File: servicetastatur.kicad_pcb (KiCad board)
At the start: 2 copper layers, 113 x 60 mm, 69 parts, among them J1 Conn_01x02, J2 LCD, J3 Automat, J4 Tasten, Q1 2N3904, U1 74HC238, U17 TL7705A, U18 MC34063AP, U2 74HC00, U3 27C128, U5 74LS573, U6 74HC4094, U7 74HC4094, U8 74HC165, U9 AT24CS16-SSHM, Y1 Crystal

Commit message: stecker
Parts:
- added C22: C, Capacitor_THT:C_Axial_L3.8mm_D2.6mm_P7.50mm_Horizontal, F.Cu at (109.2, 115.2)
- J2: footprint Connector_TE-Connectivity:TE_Micro-MaTch_1-215079-6_2x08_P1.27mm_Vertical -> adp:FFC_2x08_P1mm_Vertical
- J4: footprint Connector_Molex:Molex_Nano-Fit_105313-xx06_1x06_P2.50mm_Horizontal -> adp:FFC_1x06_P2.50mm_Horizontal
- Y1: value Crystal -> 11.059
- moved R26 22.1 mm to (168.0, 140.2), turned to 90 degrees
- moved J2 21.6 mm to (111.2, 124.8)
- moved R27 20.6 mm to (163.0, 140.2), turned to 90 degrees
- moved C19 4.54 mm to (171.0, 121.0), turned to 90 degrees
- moved C12 2.69 mm to (163.5, 122.0)
- moved J1 2.51 mm to (185.5, 118.2), turned to 180 degrees
- moved R1 1.97 mm to (90.0, 129.5)
- moved R2 1.97 mm to (103.0, 129.5)
- moved C8 1.78 mm to (89.5, 76.0)
- moved R6 1.75 mm to (118.5, 130.0)
- moved U18 1.58 mm to (135.9, 130.0)
- moved R5 1.56 mm to (118.0, 123.0)
- moved D2 1.52 mm to (118.0, 126.2)
- moved C7 1.44 mm to (146.1, 122.5)
- moved Y1 1.41 mm to (96.0, 83.5)
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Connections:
- C13 pad 1: GND -> Net-(D4-K)
- C19 pad 1: unconnected-(C19-Pad1) -> Net-(C19-Pad1)
- C21 pad 1: unconnected-(C21-Pad1) -> VCC
- C5 pad 2: Net-(U9-VCC) -> VCC
- C7 pad 2: Net-(U18-Vin) -> Net-(D3-K)
- C8 pad 1: Net-(C8-Pad1) -> GND
- C9 pad 1: Net-(C8-Pad1) -> GND
- D1 pad 1: VCC -> unconnected-(D1-K-Pad1)
- D2 pad 2: GND -> unconnected-(D2-A-Pad2)
- D4 pad 1: unconnected-(D4-K-Pad1) -> Net-(D4-K)
- D4 pad 2: unconnected-(D4-A-Pad2) -> GND
- J2 pad 13: unconnected-(J2-Pin_13-Pad13) -> Net-(J2-Pin_13)
- J2 pad 15: unconnected-(J2-Pin_15-Pad15) -> VCC
- J2 pad 2: unconnected-(J2-Pin_2-Pad2) -> Net-(J2-Pin_2)
- J2 pad 5: unconnected-(J2-Pin_5-Pad5) -> D5
- J2 pad 8: unconnected-(J2-Pin_8-Pad8) -> D2
- J3 pad 1: unconnected-(J3-Pin_1-Pad1) -> GND
- J4 pad 4: unconnected-(J4-Pin_4-Pad4) -> Net-(J4-Pin_4)
- J4 pad 5: unconnected-(J4-Pin_5-Pad5) -> Net-(J4-Pin_5)
- J4 pad 6: unconnected-(J4-Pin_6-Pad6) -> Net-(J4-Pin_6)
- Q1 pad 1: unconnected-(Q1-E-Pad1) -> Net-(D2-K)
- R1 pad 1: GND -> unconnected-(R1-Pad1)
- R10 pad 1: unconnected-(R10-Pad1) -> Net-(R10-Pad1)
- R15 pad 1: unconnected-(R15-Pad1) -> Net-(D4-K)
- R15 pad 2: unconnected-(R15-Pad2) -> GND
- R17 pad 1: unconnected-(R17-Pad1) -> CLOCK
- R18 pad 1: unconnected-(R18-Pad1) -> Net-(U7-D)
- R19 pad 2: unconnected-(R19-Pad2) -> Net-(U18-DC)
- R2 pad 2: unconnected-(R2-Pad2) -> Net-(J2-Pin_2)
- R20 pad 2: Net-(R20-Pad2) -> Net-(D3-K)
- R21 pad 2: Net-(R20-Pad2) -> Net-(D3-K)
- R22 pad 1: Net-(R20-Pad2) -> Net-(D3-K)
- R22 pad 2: Net-(C12-Pad1) -> Net-(C19-Pad1)
- R23 pad 1: unconnected-(R23-Pad1) -> Net-(C12-Pad1)
- R3 pad 2: Net-(R3-Pad2) -> Net-(U18-Vfb)
- R4 pad 2: Net-(R3-Pad2) -> Net-(U18-Vfb)
- U1 pad 6: unconnected-(U1-E3-Pad6) -> Net-(U1-E3)
- U18 pad 2: GND -> unconnected-(U18-SwE-Pad2)
- U18 pad 5: unconnected-(U18-Vfb-Pad5) -> Net-(U18-Vfb)
- U18 pad 6: Net-(U18-Vin) -> Net-(D3-K)
- U18 pad 8: unconnected-(U18-DC-Pad8) -> Net-(U18-DC)
- U2 pad 1: Net-(U2-Pad1) -> Net-(R10-Pad1)
- U2 pad 12: GND -> Net-(U4-P3.3/INT1)
- U2 pad 13: Net-(U2-Pad13) -> Net-(U4-P3.3/INT1)
- U2 pad 2: Net-(U2-Pad1) -> Net-(R10-Pad1)
- U2 pad 3: Net-(U2-Pad13) -> Net-(U4-P3.3/INT1)
- U2 pad 8: unconnected-(U2-Pad8) -> Net-(U1-E3)
- U3 pad 1: unconnected-(U3-VPP-Pad1) -> A15
- U3 pad 27: unconnected-(U3-~{PGM}-Pad27) -> A14
- U3 pad 9: Net-(U3-A1) -> Net-(J2-Pin_13)
- U4 pad 15: unconnected-(U4-P3.3/INT1-Pad15) -> Net-(U4-P3.3/INT1)
- U4 pad 6: unconnected-(U4-P1.4-Pad6) -> Net-(J4-Pin_4)
- U4 pad 7: unconnected-(U4-P1.5-Pad7) -> Net-(J4-Pin_5)
- U4 pad 8: unconnected-(U4-P1.6-Pad8) -> Net-(J4-Pin_6)
- U5 pad 13: Net-(U3-A1) -> Net-(J2-Pin_13)
- U6 pad 1: unconnected-(U6-STR-Pad1) -> Net-(U6-STR)
- U6 pad 3: Net-(U6-CP) -> CLOCK
- U7 pad 1: unconnected-(U7-STR-Pad1) -> Net-(U6-STR)
- U7 pad 2: unconnected-(U7-D-Pad2) -> Net-(U7-D)
- U7 pad 3: Net-(U6-CP) -> CLOCK
- U8 pad 2: unconnected-(U8-CP-Pad2) -> CLOCK
- U9 pad 1: unconnected-(U9-NC-Pad1) -> GND
- U9 pad 2: unconnected-(U9-NC-Pad2) -> GND
- U9 pad 3: unconnected-(U9-NC-Pad3) -> GND
- U9 pad 8: Net-(U9-VCC) -> VCC
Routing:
- net GND: track 134.8 -> 520.2 mm, vias 2 -> 7
- net VCC: track 102.6 -> 299.1 mm, vias 0 -> 2
- net Net-(R10-Pad1): track 0.00 -> 110.7 mm, vias 0 -> 2
- net D5: track 42.8 -> 120.3 mm, vias 2 -> 4
- net CLOCK: track 0.00 -> 69.5 mm, vias 0 -> 2
- net Net-(D3-K): track 9.69 -> 73.0 mm
- net Net-(U1-E3): track 0.00 -> 56.6 mm, vias 0 -> 2
- net (no net): track 52.4 -> 0.00 mm, vias 2 -> 0
- net Net-(U4-P3.3/INT1): track 0.00 -> 50.2 mm, vias 0 -> 1
- net RESET: track 0.00 -> 46.5 mm
- net D4: track 45.5 -> 90.0 mm
- net D6: track 52.3 -> 96.7 mm
- net D0: track 86.5 -> 125.8 mm
- net Net-(J2-Pin_2): track 0.00 -> 38.4 mm, vias 0 -> 1
- net Net-(J4-Pin_2): track 0.00 -> 36.8 mm
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- removed copper zone on B.Cu, net GND
- removed copper zone on B.Cu, net VCC
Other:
- board size 113 x 60 mm -> 113.2 x 58 mm

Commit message: spekulation
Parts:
- moved R11 0.66 mm to (167.2, 84.0)
- moved R7 0.66 mm to (167.2, 86.5)
- moved R8 0.66 mm to (167.2, 89.0)
- moved R9 0.66 mm to (167.2, 91.8)
- moved C12 0.46 mm to (164.0, 122.0)
- moved R23 0.41 mm to (156.8, 118.0)
- moved U18 0.37 mm to (136.2, 130.0)
- moved R12 0.35 mm to (148.8, 75.8)
- moved R24 0.35 mm to (92.8, 101.2)
- moved R25 0.35 mm to (77.8, 101.2)
- moved U17 0.35 mm to (156.2, 83.2)
- moved R13 0.34 mm to (138.5, 78.0)
- moved U4 0.33 mm to (116.2, 87.2)
- moved U9 0.28 mm to (125.2, 83.2)
- moved D4 0.27 mm to (171.2, 94.5)
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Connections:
- C11 pad 2: Net-(C11-Pad2) -> RESET
- D1 pad 1: unconnected-(D1-K-Pad1) -> VCC
- R12 pad 2: Net-(C11-Pad2) -> RESET
- R13 pad 1: Net-(C11-Pad2) -> RESET
- U1 pad 1: unconnected-(U1-A0-Pad1) -> Net-(U1-A0)
- U1 pad 2: unconnected-(U1-A1-Pad2) -> Net-(U1-A1)
- U1 pad 3: unconnected-(U1-A2-Pad3) -> Net-(U1-A2)
- U3 pad 4: Net-(U3-A6) -> Net-(U1-A2)
- U3 pad 5: Net-(U3-A5) -> Net-(U1-A1)
- U3 pad 6: Net-(U3-A4) -> Net-(U1-A0)
- U5 pad 16: Net-(U3-A4) -> Net-(U1-A0)
- U5 pad 17: Net-(U3-A5) -> Net-(U1-A1)
- U5 pad 18: Net-(U3-A6) -> Net-(U1-A2)
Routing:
- net Net-(U1-A1): track 0.00 -> 44.3 mm
- net Net-(U1-A2): track 0.00 -> 35.0 mm, vias 0 -> 1
- net Net-(U3-A5): track 32.6 -> 0.00 mm
- net Net-(U1-A0): track 0.00 -> 26.0 mm
- net A15: track 28.0 -> 48.3 mm
- net unconnected-(R1-Pad1): track 0.00 -> 19.3 mm
- net A14: track 54.4 -> 69.9 mm
- net Net-(U3-A6): track 12.1 -> 0.00 mm
- net Net-(U3-A4): track 12.1 -> 0.00 mm
- net unconnected-(J2-Pin_11-Pad11): track 19.0 -> 29.2 mm
- net unconnected-(U1-A2-Pad3): track 8.21 -> 0.00 mm, vias 1 -> 0
- net SDA: track 30.9 -> 26.5 mm
- net Net-(C12-Pad1): track 24.5 -> 28.0 mm
- net GND: track 520.2 -> 521.8 mm
- net Net-(J3-Pin_5): track 27.5 -> 28.5 mm
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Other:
- board size 113.2 x 58 mm -> 113.9 x 58 mm

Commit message: layout
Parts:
- added R28: R, Resistor_THT:R_Axial_DIN0207_L6.3mm_D2.5mm_P10.16mm_Horizontal, F.Cu at (132.7, 87.6)
- added R29: R, Resistor_THT:R_Axial_DIN0207_L6.3mm_D2.5mm_P10.16mm_Horizontal, F.Cu at (130.2, 87.6)
- added R30: R, Resistor_THT:R_Axial_DIN0207_L6.3mm_D2.5mm_P10.16mm_Horizontal, F.Cu at (127.5, 87.6)
- C1: footprint Capacitor_THT:CP_Radial_D5.0mm_P2.00mm -> Capacitor_THT:CP_Radial_D5.0mm_P2.50mm
- C3: renamed from C13; value C -> 68pF
- D1: footprint Diode_THT:D_DO-15_P15.24mm_Horizontal -> adp:D_DO-15_P15mm_Horizontal
- Q1: footprint Package_TO_SOT_THT:TO-92 -> adp:TO-92
- R15: renamed from R3; value 110 Ω ±1% -> 1 kΩ ±1%
- R26, R27: value 100 kΩ ±5% -> R
- R6: value R -> 220 Ω ±5%
- U4: value ~ -> 80C31
- U9: value AT24CS16-SSHM -> 24CS16
- moved Y1 49.5 mm to (70.5, 41.0)
- moved C21 49.5 mm to (100.3, 45.4)
- moved C1 49.5 mm to (91.6, 62.9)
- moved C10 49.5 mm to (141.6, 36.0)
- moved C11 49.5 mm to (127.1, 35.8)
- moved C12 49.5 mm to (138.6, 79.5)
- moved C13 49.5 mm to (96.6, 62.0)
- moved C14 49.5 mm to (135.1, 51.0)
- moved C15 49.5 mm to (119.6, 62.0)
- moved C16 49.5 mm to (119.6, 73.0)
- moved C17 49.5 mm to (96.6, 73.0)
- moved C18 49.5 mm to (83.1, 57.5)
- moved C19 49.5 mm to (145.6, 78.5)
- moved C2 49.5 mm to (91.4, 69.5)
- moved C20 49.5 mm to (138.1, 46.0)
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- renumbered C3 to C13, R15 to R3
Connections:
- net Net-(J2-Pin_13) renamed A1
- net Net-(U1-A0) renamed A4
- net Net-(U1-A1) renamed A5
- net Net-(U1-A2) renamed A6
- net Net-(U3-A2) renamed A2
- net Net-(U3-A3) renamed A3
- net Net-(U3-A7) renamed A7
- C10 pad 2: unconnected-(C10-Pad2) -> Net-(U17-CT)
- C3 pad 2: unconnected-(C13-Pad2) -> Net-(J3-Pin_3)
- C7 pad 2: Net-(D3-K) -> Net-(U18-TC)
- D2 pad 2: unconnected-(D2-A-Pad2) -> GND
- D3 pad 1: Net-(D3-K) -> +VDC
- J2 pad 10: unconnected-(J2-Pin_10-Pad10) -> D0
- J2 pad 11: unconnected-(J2-Pin_11-Pad11) -> Net-(J2-Pin_11)
- J2 pad 12: unconnected-(J2-Pin_12-Pad12) -> A0
- J2 pad 16: unconnected-(J2-Pin_16-Pad16) -> GND
- J2 pad 2: Net-(J2-Pin_2) -> GND
- J2 pad 3: unconnected-(J2-Pin_3-Pad3) -> D7
- J2 pad 4: unconnected-(J2-Pin_4-Pad4) -> D6
- J2 pad 6: unconnected-(J2-Pin_6-Pad6) -> D4
- R1 pad 1: unconnected-(R1-Pad1) -> GND
- R2 pad 2: Net-(J2-Pin_2) -> GND
- R20 pad 2: Net-(D3-K) -> +VDC
- R21 pad 2: Net-(D3-K) -> +VDC
- R22 pad 1: Net-(D3-K) -> +VDC
- R23 pad 2: Net-(D3-K) -> +VDC
- R5 pad 1: unconnected-(R5-Pad1) -> Net-(Q1-C)
- U1 pad 7: unconnected-(U1-Y7-Pad7) -> Net-(J2-Pin_11)
- U17 pad 3: unconnected-(U17-CT-Pad3) -> Net-(U17-CT)
- U18 pad 2: unconnected-(U18-SwE-Pad2) -> GND
- U18 pad 3: unconnected-(U18-TC-Pad3) -> Net-(U18-TC)
- U18 pad 6: Net-(D3-K) -> +VDC
- U3 pad 10: Net-(U3-A0) -> A0
- U5 pad 12: Net-(U3-A0) -> A0
- U6 pad 1: Net-(U6-STR) -> Net-(D4-K)
- U7 pad 1: Net-(U6-STR) -> Net-(D4-K)
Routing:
- net GND: track 521.8 -> 698.4 mm, vias 7 -> 8
- net Net-(D3-K): track 73.3 -> 0.00 mm, vias 1 -> 0
- net +VDC: track 0.00 -> 72.9 mm, vias 0 -> 1
- net D7: track 92.8 -> 159.8 mm, vias 3 -> 4
- net D6: track 97.1 -> 159.6 mm, vias 3 -> 4
- net D4: track 90.0 -> 146.1 mm, vias 2 -> 3
- net A15: track 48.3 -> 98.3 mm
- net Net-(J2-Pin_11): track 0.00 -> 42.9 mm
- net Net-(J2-Pin_2): track 38.3 -> 0.00 mm, vias 1 -> 0
- net A0: track 0.00 -> 34.6 mm
- net Net-(D4-K): track 22.5 -> 56.4 mm, vias 0 -> 1
- net unconnected-(J2-Pin_11-Pad11): track 29.2 -> 0.00 mm
- net A14: track 69.9 -> 97.7 mm
- net A6: track 35.0 -> 62.1 mm
- net unconnected-(J2-Pin_6-Pad6): track 25.5 -> 0.00 mm, vias 1 -> 0
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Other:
- outline, holes or cut-outs redrawn
- board text added: "https://github.com/stonedDiscord/"
- board text added: "servicetastatur"
- board text removed: "8320/00020f/DN"
- board text removed: "stwirtxt"

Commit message: so hab bestellt
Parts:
- removed R26, R27, R28, R29, R30: R, Resistor_THT:R_Axial_DIN0207_L6.3mm_D2.5mm_P10.16mm_Horizontal
- added J5: Conn_01x03_Pin, Connector_PinSocket_2.54mm:PinSocket_1x03_P2.54mm_Vertical, F.Cu at (127.5, 87.6)
- added J6: Conn_01x03_Pin, Connector_PinSocket_2.54mm:PinSocket_1x03_P2.54mm_Vertical, F.Cu at (137.6, 87.6)
- R20, R21, R22: value 100 kΩ ±5% -> 1 Ω ±5%
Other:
- board text added: "JLCJLCJLCJLC"

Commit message: deko
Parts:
- D1, D3: value D -> 1N5819
- R1, R4: value 3.3 kΩ ±5% -> 3.3 kΩ
- R10, R14, R15, R7, R8, R9: value 1 kΩ ±1% -> 1 kΩ
- R11: value 10 kΩ ±5% -> 10 kΩ
- R12, R2: value 22 Ω ±5% -> 22 Ω
- R13: value 47 kΩ ±5% -> 47 kΩ
- R16: value 47 Ω ±1% -> 47 Ω
- R17, R18, R19, R5: value 270 Ω ±5% -> 270 Ω
- R20, R21, R22: value 1 Ω ±5% -> 1 Ω
- R23: value 100 Ω ±1% -> 100 Ω
- R24: value 100 kΩ ±5% -> 100 kΩ
- R25, R3: value 4.7 kΩ ±1% -> 4.7 kΩ
- R6: value 220 Ω ±5% -> 220 Ω
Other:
- outline, holes or cut-outs redrawn

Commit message: lcd gefixt
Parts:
- moved J2 15.1 mm to (71.1, 84.2), turned to 90 degrees
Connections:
- J2 pad 10: D0 -> D3
- J2 pad 11: Net-(J2-Pin_11) -> D4
- J2 pad 12: A0 -> D5
- J2 pad 13: A1 -> D6
- J2 pad 14: Net-(J2-Pin_14) -> D7
- J2 pad 2: GND -> VCC
- J2 pad 3: D7 -> Net-(J2-Pin_3)
- J2 pad 4: D6 -> A1
- J2 pad 5: D5 -> A0
- J2 pad 6: D4 -> Net-(J2-Pin_6)
- J2 pad 7: D3 -> D0
- J2 pad 8: D2 -> D1
- J2 pad 9: D1 -> D2
- R1 pad 1: GND -> VCC
- R1 pad 2: Net-(J2-Pin_14) -> Net-(J2-Pin_3)
- R2 pad 2: GND -> VCC
- U1 pad 7: Net-(J2-Pin_11) -> Net-(J2-Pin_6)
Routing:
- net GND: track 698.2 -> 617.7 mm, vias 8 -> 7
- net VCC: track 317.5 -> 377.2 mm, vias 2 -> 3
- net Net-(J2-Pin_6): track 0.00 -> 42.9 mm
- net Net-(J2-Pin_11): track 42.9 -> 0.00 mm
- net Net-(J2-Pin_3): track 0.00 -> 3.54 mm
- net Net-(J2-Pin_14): track 3.54 -> 0.00 mm

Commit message: kompakt
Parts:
- removed C12: C_Polarized, Capacitor_THT:CP_Radial_D5.0mm_P2.00mm
- removed C19: C, Capacitor_THT:CP_Radial_Tantal_D4.5mm_P2.50mm
- removed C7: C, Capacitor_THT:C_Axial_L3.8mm_D2.6mm_P7.50mm_Horizontal
- removed D2: D, Diode_THT:D_DO-15_P15.24mm_Horizontal
- removed J1: Conn_01x02, Connector_Wire:SolderWire-0.5sqmm_1x02_P4.8mm_D0.9mm_OD2.3mm
- removed J4: Tasten, adp:FFC_1x06_P2.50mm_Horizontal
- removed J5, J6: Conn_01x03_Pin, Connector_PinSocket_2.54mm:PinSocket_1x03_P2.54mm_Vertical
- removed Q1: 2N3904, adp:TO-92
- removed R12, R2: 22 Ω, Resistor_THT:R_Axial_DIN0207_L6.3mm_D2.5mm_P10.16mm_Horizontal
- removed R15: 1 kΩ, Resistor_THT:R_Axial_DIN0207_L6.3mm_D2.5mm_P10.16mm_Horizontal
- removed R19, R5: 270 Ω, Resistor_THT:R_Axial_DIN0207_L6.3mm_D2.5mm_P10.16mm_Horizontal
- removed R20, R21, R22: 1 Ω, Resistor_THT:R_Axial_DIN0207_L6.3mm_D2.5mm_P10.16mm_Horizontal
- removed R23: 100 Ω, Resistor_THT:R_Axial_DIN0207_L6.3mm_D2.5mm_P10.16mm_Horizontal
- removed R24: 100 kΩ, Resistor_THT:R_Axial_DIN0207_L6.3mm_D2.5mm_P10.16mm_Horizontal
- removed R4: 3.3 kΩ, Resistor_THT:R_Axial_DIN0207_L6.3mm_D2.5mm_P10.16mm_Horizontal
- removed R6: 220 Ω, Resistor_THT:R_Axial_DIN0414_L11.9mm_D4.5mm_P15.24mm_Horizontal
- removed U18: MC34063AP, Package_DIP:DIP-8_W7.62mm
- removed U4: 80C31, Package_LCC:PLCC-44_THT-Socket
- removed U5: 74LS573, Package_DIP:DIP-20_W7.62mm
- removed U6, U7: 74HC4094, Package_DIP:DIP-16_W7.62mm
- removed U8: 74HC165, Package_DIP:DIP-16_W7.62mm
- removed U9: 24CS16, Package_DIP:DIP-8_W7.62mm
- added F1: Fuse, Fuse:Fuse_0805_2012Metric, F.Cu at (185.4, 34.6)
- added RV1: Kontrast, Potentiometer_THT:Potentiometer_ACP_CA9-V10_Vertical_Hole, F.Cu at (25.6, 50.8)
- added RV2: Helligkeit, Potentiometer_THT:Potentiometer_ACP_CA9-V10_Vertical_Hole, F.Cu at (24.2, 23.0)
- added SW1: OK, Button_Switch_THT:SW_PUSH_6mm, F.Cu at (181.6, 68.6)
- added SW2: →, Button_Switch_THT:SW_PUSH_6mm, F.Cu at (37.4, 66.3)
- added SW3: F3, Button_Switch_THT:SW_PUSH_6mm, F.Cu at (119.4, 72.4)
- added SW4: F4, Button_Switch_THT:SW_PUSH_6mm, F.Cu at (144.8, 72.4)
- added SW5: ←, Button_Switch_THT:SW_PUSH_6mm, F.Cu at (17.1, 66.3)
- added SW6: F1, Button_Switch_THT:SW_PUSH_6mm, F.Cu at (68.6, 72.4)
- added SW7: ↑, Button_Switch_THT:SW_PUSH_6mm, F.Cu at (27.2, 58.7)
- added SW8: ↓, Button_Switch_THT:SW_PUSH_6mm, F.Cu at (27.2, 74.0)
- added SW9: F2, Button_Switch_THT:SW_PUSH_6mm, F.Cu at (94.0, 72.4)
- added U11: 80C31, Package_LCC:PLCC-44_THT-Socket, F.Cu at (109.2, 31.2)
- added U12: 74LS573, Package_SO:SOIC-20W_7.5x12.8mm_P1.27mm, F.Cu at (154.3, 50.4)
- added U13: 74HC165, Package_SO:SOIC-16W_5.3x10.2mm_P1.27mm, F.Cu at (47.5, 48.9)
- added U15: 24CS16, Package_SO:SO-8_3.9x4.9mm_P1.27mm, F.Cu at (88.9, 32.4)
- added U16: 74HC238, Package_SO:SOIC-16W_5.3x10.2mm_P1.27mm, F.Cu at (137.2, 50.8)
- added U19: 74HC4094, Package_SO:SOIC-16W_5.3x10.2mm_P1.27mm, F.Cu at (126.3, 33.0)
- added U20: 74HC4094, Package_SO:SOIC-16W_5.3x10.2mm_P1.27mm, F.Cu at (174.6, 57.9)
- added Y2: 11.059, Crystal:Crystal_SMD_HC49-SD, F.Cu at (97.3, 55.9)
- C1: value C_Polarized -> 1uF; footprint Capacitor_THT:CP_Radial_D5.0mm_P2.50mm -> Capacitor_SMD:C_1206_3216Metric
- C10: value C -> 0,1uF; footprint Capacitor_THT:CP_Radial_Tantal_D4.5mm_P2.50mm -> Capacitor_SMD:C_0603_1608Metric
- C11: footprint Capacitor_THT:CP_Radial_Tantal_D4.5mm_P2.50mm -> Capacitor_SMD:C_0805_2012Metric
- C13, C14, C15, C16, C17, C18, C22, C5: value C -> 100nF; footprint Capacitor_THT:C_Axial_L3.8mm_D2.6mm_P7.50mm_Horizontal -> Capacitor_SMD:C_0603_1608Metric
- C2: value C_Polarized -> 1uF; footprint Capacitor_THT:CP_Radial_D5.0mm_P2.00mm -> Capacitor_SMD:C_1206_3216Metric
- C20, C21: value C -> 100nF; footprint Capacitor_THT:CP_Radial_Tantal_D4.5mm_P2.50mm -> Capacitor_SMD:C_0603_1608Metric
- C3: footprint Capacitor_THT:C_Axial_L3.8mm_D2.6mm_P7.50mm_Horizontal -> Capacitor_SMD:C_0603_1608Metric
- C4: value C -> 1uF; footprint Capacitor_THT:C_Axial_L3.8mm_D2.6mm_P7.50mm_Horizontal -> Capacitor_SMD:C_0603_1608Metric
- C6: value C -> 0,1uF; footprint Capacitor_THT:C_Axial_L3.8mm_D2.6mm_P7.50mm_Horizontal -> Capacitor_SMD:C_0603_1608Metric
- C8, C9: value C -> 33pF; footprint Capacitor_THT:CP_Radial_Tantal_D4.5mm_P2.50mm -> Capacitor_SMD:C_0603_1608Metric
- D1: value 1N5819 -> LED; footprint adp:D_DO-15_P15mm_Horizontal -> LED_SMD:LED_0603_1608Metric
- D3: footprint Diode_THT:D_DO-15_P15.24mm_Horizontal -> Diode_SMD:D_2010_5025Metric
- D4: footprint Diode_THT:D_A-405_P7.62mm_Horizontal -> Diode_SMD:D_0805_2012Metric
- J2: value LCD -> Conn_02x08_Odd_Even_MountingPin; footprint adp:FFC_2x08_P1mm_Vertical -> ConnPad:LCDdisplay
- R1: value 3.3 kΩ -> 470; footprint Resistor_THT:R_Axial_DIN0207_L6.3mm_D2.5mm_P10.16mm_Horizontal -> Resistor_SMD:R_0603_1608Metric
- R10, R11, R14, R16, R17, R18, R25, R3, R7, R8, R9: footprint Resistor_THT:R_Axial_DIN0207_L6.3mm_D2.5mm_P10.16mm_Horizontal -> Resistor_SMD:R_0603_1608Metric
- R13: footprint Resistor_THT:R_Axial_DIN0207_L6.3mm_D2.5mm_P10.16mm_Horizontal -> Resistor_SMD:R_0805_2012Metric
- U1: value 74HC238 -> ~; footprint Package_DIP:DIP-16_W7.62mm -> Package_DIP:DIP-40_W15.24mm
- U17: footprint Package_DIP:DIP-8_W7.62mm -> Package_SO:SO-8_3.9x4.9mm_P1.27mm
- U2: footprint Package_DIP:DIP-14_W7.62mm -> Package_SO:SOIC-14_3.9x8.7mm_P1.27mm
- moved R1 129.4 mm to (192.0, 62.9), turned to 180 degrees
- moved D1 98.1 mm to (187.8, 62.9), turned to 180 degrees
- moved C15 97.6 mm to (22.9, 49.2)
- moved U3 88.2 mm to (133.3, 39.4)
- moved C17 87.1 mm to (182.9, 61.0), turned to 180 degrees
- moved R25 84.1 mm to (135.0, 43.2)
- moved U1 72.6 mm to (34.3, 40.6)
- moved C11 69.7 mm to (58.1, 45.7), turned to 180 degrees
- moved C16 69.1 mm to (52.4, 57.1), turned to 0 degrees
- moved C18 60.1 mm to (143.2, 57.1), turned to 180 degrees
- moved R14 57.0 mm to (40.6, 56.2), turned to -90 degrees
- moved J2 55.8 mm to (101.8, 37.5), turned to 0 degrees
- moved D3 52.5 mm to (185.4, 40.9), turned to -90 degrees
- moved C8 49.9 mm to (108.9, 55.9), turned to 180 degrees
- moved C2 46.3 mm to (46.8, 57.1), turned to 0 degrees
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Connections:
- C8 pad 2: Net-(U4-XTAL2) -> Net-(U1-XTAL2)
- C9 pad 2: Net-(U4-XTAL1) -> Net-(U1-XTAL1)
- D1 pad 1: VCC -> Net-(D1-K)
- D1 pad 2: Net-(D1-A) -> VCC
- J2 pad 15: VCC -> /Helligkeit
- J2 pad 3: Net-(J2-Pin_3) -> /Kontrast
- J2 pad 6: Net-(J2-Pin_6) -> /LCD_EN
- R1 pad 1: VCC -> GND
- R1 pad 2: Net-(J2-Pin_3) -> Net-(D1-K)
- R11 pad 1: Net-(U17-~{RESIN}) -> GND
- R11 pad 2: VCC -> RESET
- R25 pad 2: Net-(R24-Pad1) -> A15
- U1 pad 1: A4 -> Net-(U1-P1.0)
- U1 pad 10: Net-(U1-Y5) -> unconnected-(U1-P3.0/RxD-Pad10)
- U1 pad 11: Net-(U1-Y4) -> unconnected-(U1-P3.1/TxD-Pad11)
- U1 pad 12: unconnected-(U1-Y3-Pad12) -> Net-(U1-P3.2/INT0)
- U1 pad 13: unconnected-(U1-Y2-Pad13) -> Net-(U1-P3.3/INT1)
- U1 pad 14: unconnected-(U1-Y1-Pad14) -> SDA
- U1 pad 15: unconnected-(U1-Y0-Pad15) -> SCL
- U1 pad 16: VCC -> Net-(U1-P3.6/WR)
- U1 pad 2: A5 -> Net-(U1-P1.1)
- U1 pad 3: A6 -> Net-(U1-P1.2)
- U1 pad 4: A14 -> unconnected-(U1-P1.3-Pad4)
- U1 pad 5: A15 -> Net-(U1-P1.4)
- U1 pad 6: Net-(U1-E3) -> Net-(U1-P1.5)
- U1 pad 7: Net-(J2-Pin_6) -> Net-(U1-P1.6)
- U1 pad 8: GND -> unconnected-(U1-P1.7-Pad8)
- U1 pad 9: Net-(U1-Y6) -> RESET
- U17 pad 2: Net-(U17-~{RESIN}) -> VCC
- U17 pad 6: Net-(U17-RESET) -> RESET
- U2 pad 10: Net-(U4-P3.6/WR) -> Net-(U1-P3.6/WR)
- U2 pad 11: Net-(U4-P3.2/INT0) -> Net-(U1-P3.2/INT0)
- U2 pad 12: Net-(U4-P3.3/INT1) -> Net-(U1-P3.3/INT1)
- U2 pad 13: Net-(U4-P3.3/INT1) -> Net-(U1-P3.3/INT1)
- U2 pad 3: Net-(U4-P3.3/INT1) -> Net-(U1-P3.3/INT1)
- U2 pad 4: Net-(U1-Y6) -> Net-(U16-Y6)
- U2 pad 5: Net-(U1-Y6) -> Net-(U16-Y6)
- U2 pad 8: Net-(U1-E3) -> Net-(U16-E3)
- U2 pad 9: Net-(U4-P3.7/RD) -> Net-(U1-P3.7/RD)
- U3 pad 2: Net-(U3-A12) -> Net-(U1-P2.4/A12)
- U3 pad 20: Net-(U3-~{CE}) -> Net-(U1-PSEN)
- U3 pad 21: Net-(U3-A10) -> Net-(U1-P2.2/A10)
- U3 pad 22: Net-(U3-~{CE}) -> Net-(U1-PSEN)
- U3 pad 23: Net-(U3-A11) -> Net-(U1-P2.3/A11)
- U3 pad 24: Net-(U3-A9) -> Net-(U1-P2.1/A9)
- U3 pad 25: Net-(U3-A8) -> Net-(U1-P2.0/A8)
- U3 pad 26: Net-(U3-A13) -> Net-(U1-P2.5/A13)
- Y1 pad 1: Net-(U4-XTAL1) -> Net-(U1-XTAL1)
- Y1 pad 2: Net-(U4-XTAL2) -> Net-(U1-XTAL2)
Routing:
- net Net-(U1-P1.5): track 0.00 -> 243.4 mm, vias 0 -> 1
- net Net-(U1-P1.4): track 0.00 -> 236.4 mm, vias 0 -> 2
- net Net-(U1-P1.0): track 0.00 -> 226.3 mm, vias 0 -> 1
- net Net-(U1-P1.6): track 0.00 -> 190.0 mm, vias 0 -> 1
- net D4: track 146.1 -> 312.2 mm, vias 3 -> 5
- net Net-(U1-P2.2/A10): track 0.00 -> 164.4 mm, vias 0 -> 3
- net Net-(U1-P1.2): track 0.00 -> 161.1 mm, vias 0 -> 1
- net A1: track 18.0 -> 177.9 mm, vias 0 -> 2
- net CLOCK: track 69.8 -> 227.9 mm, vias 2 -> 4
- net D5: track 140.3 -> 297.1 mm, vias 4 -> 6
- net /LCD_EN: track 0.00 -> 153.0 mm, vias 0 -> 3
- net D0: track 130.0 -> 279.2 mm, vias 1 -> 6
- net Net-(U1-P1.1): track 0.00 -> 149.2 mm, vias 0 -> 3
- net A0: track 34.6 -> 176.2 mm, vias 0 -> 2
- net D3: track 114.5 -> 252.3 mm, vias 2 -> 4
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- added copper zone on B.Cu, net GND
- added copper zone on F.Cu, net GND
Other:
- board size 113.9 x 58 mm -> 185.4 x 62.2 mm
- board text added: "1"
- board text added: "16"
- board text added: "GND"
- board text added: "Kabel"
- board text added: "Kabel binder"
- board text added: "VCC"
- board text removed: "JLCJLCJLCJLC"
- board text removed: "https://github.com/stonedDiscord/"
- board text removed: "servicetastatur"

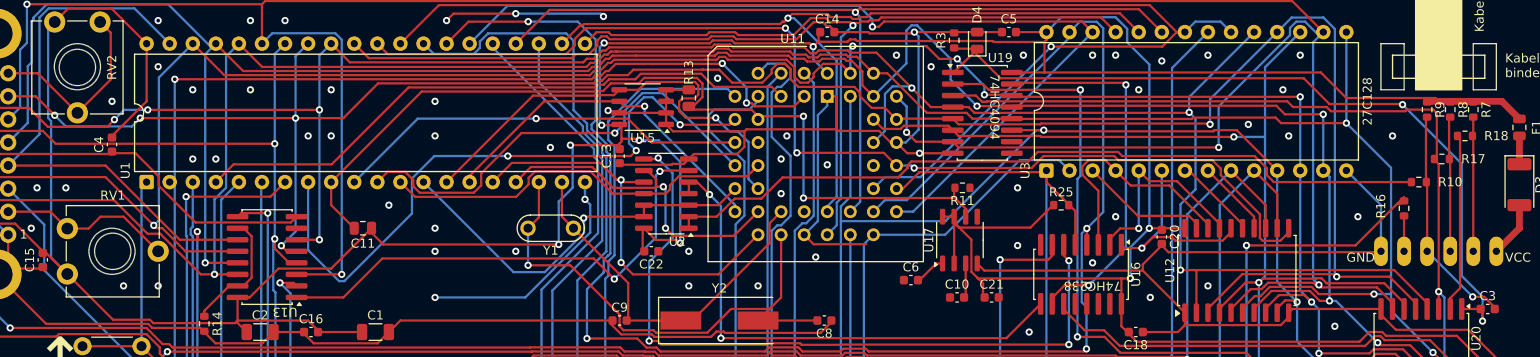
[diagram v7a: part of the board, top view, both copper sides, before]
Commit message: replace reset circuit with cap
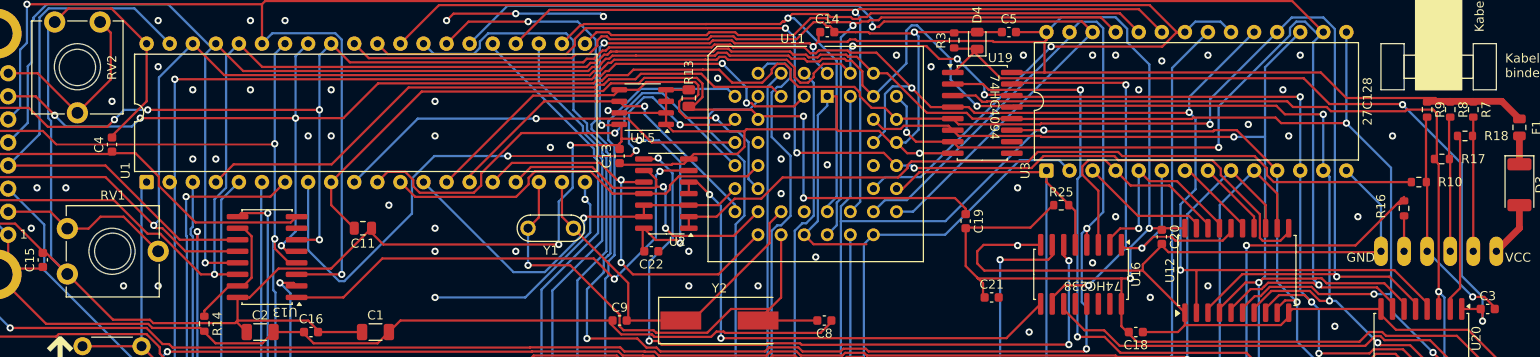
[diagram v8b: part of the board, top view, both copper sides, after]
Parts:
- removed C10, C6: 0,1uF, Capacitor_SMD:C_0603_1608Metric
- removed R11: 10 kΩ, Resistor_SMD:R_0603_1608Metric
- removed U17: TL7705A, Package_SO:SO-8_3.9x4.9mm_P1.27mm
- added C19: 1uF, Capacitor_SMD:C_0603_1608Metric, F.Cu at (124.5, 44.9)
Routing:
- net VCC: track 466.0 -> 456.4 mm
- net GND: track 548.4 -> 557.0 mm
- net Net-(U17-CT): track 3.74 -> 0.00 mm
- net Net-(U17-REF): track 3.30 -> 0.00 mm
- net RESET: track 98.2 -> 97.1 mm
